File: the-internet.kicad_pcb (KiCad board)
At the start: 2 copper layers, 88 x 40 mm, 11 parts, among them J1 POWER, J2 LOLIN-C3-MINI (L), J3 LOLIN-C3-MINI (R), Q1 KSC1815YTA

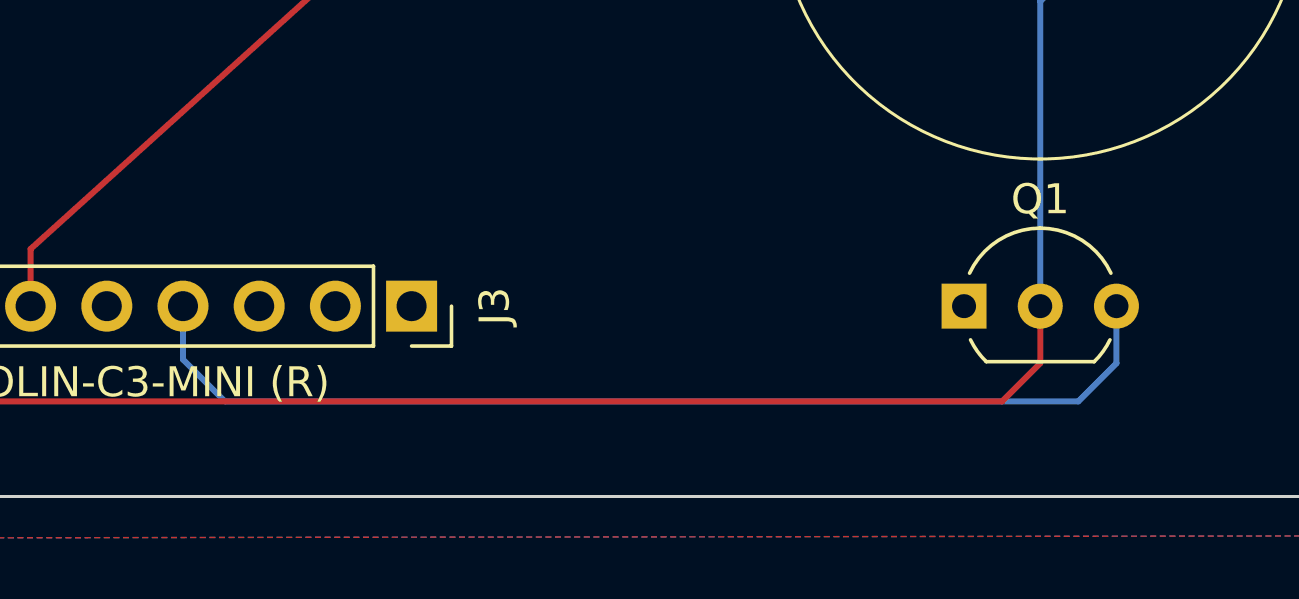
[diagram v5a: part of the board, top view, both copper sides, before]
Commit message: Add resistor to buzzer transistor
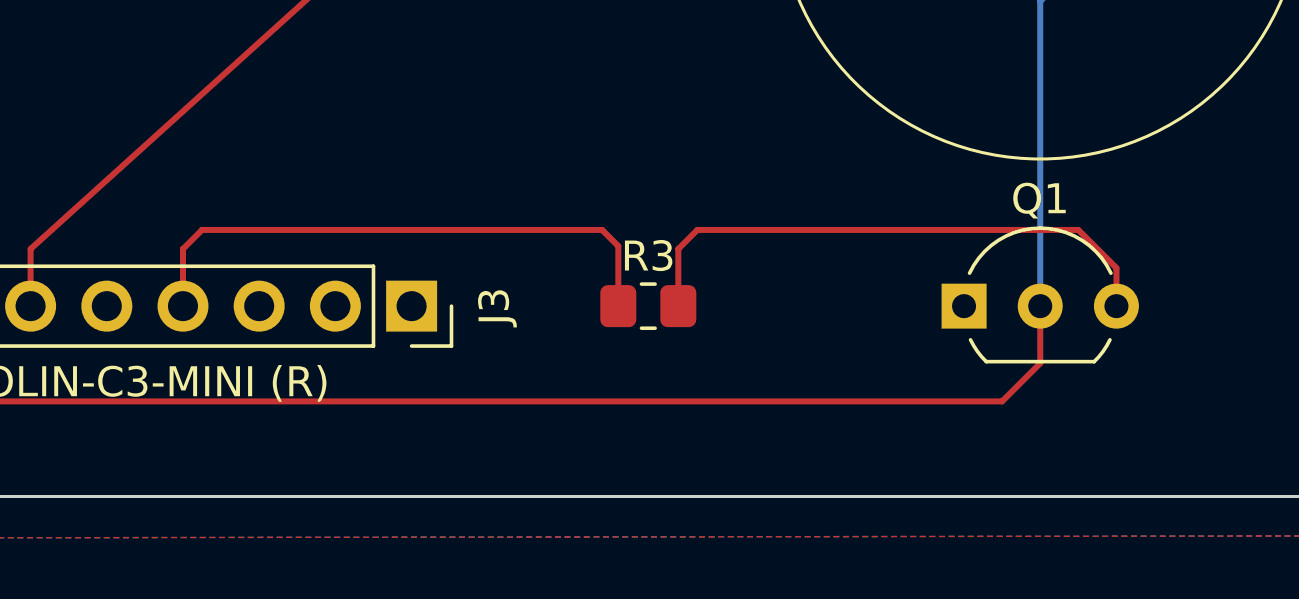
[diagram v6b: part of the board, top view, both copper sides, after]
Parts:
- added R3: 47kΩ 1% 125mW, Resistor_SMD:R_0805_2012Metric_Pad1.20x1.40mm_HandSolder, F.Cu at (64.4, 59.1)
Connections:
- Q1 pad 3: BUZZER/GPIO8 -> Net-(Q1-B)
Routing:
- net Net-(Q1-B): track 0.00 -> 18.6 mm
- net BUZZER/GPIO8: track 35.9 -> 18.9 mm
